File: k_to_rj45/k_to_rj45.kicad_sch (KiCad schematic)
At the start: 10 parts, among them J1 Conn_01x01_Female, J2 Conn_01x01_Female, J3 Conn_01x01_Female, J4 Conn_01x01_Female, J5 Conn_01x01_Female, J6 RJ45_Shielded, J7 Conn_01x01_Female, J8 Conn_01x01_Female

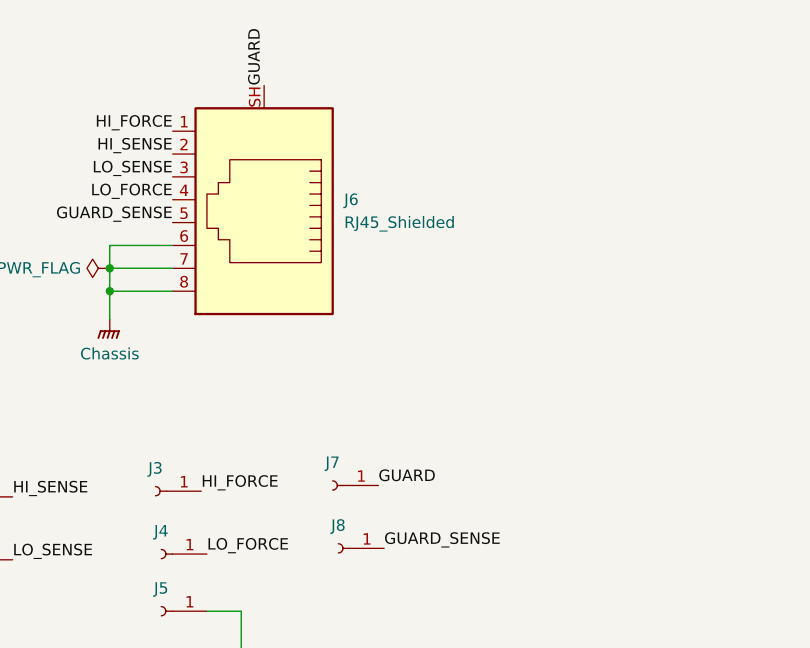
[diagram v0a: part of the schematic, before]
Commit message: update rj45 adapter and contact checker to v2
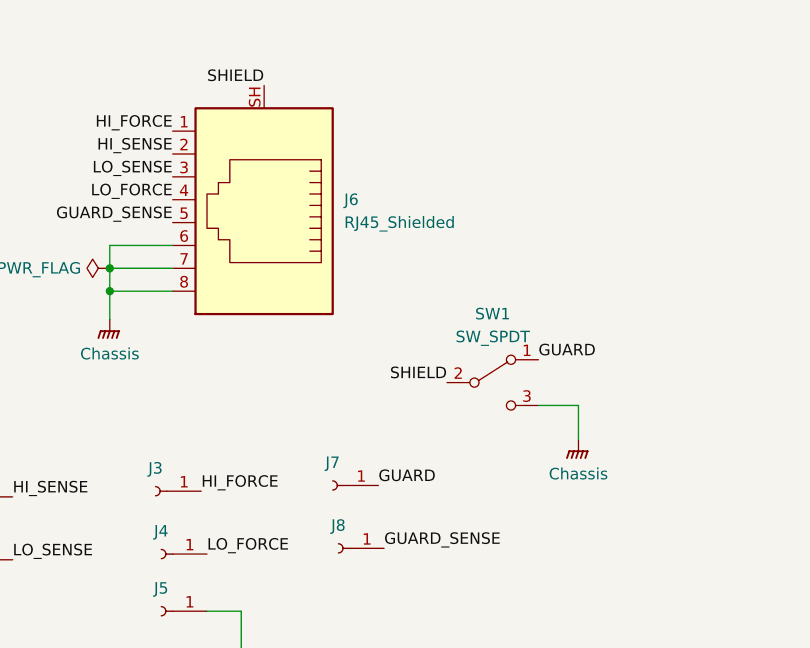
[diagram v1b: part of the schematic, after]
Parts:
- added SW1: SW_SPDT, custom_footprints:SPDT_slide_switch, symbol Switch:SW_SPDT
- J6: footprint Connector_RJ:RJ45_Wuerth_7499010001A_Horizontal -> custom_footprints:RJ45_TE_5557969-1_vertical_shield
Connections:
- net GNDPWR: now also SW1.3 (C)
- net GUARD: now also SW1.1 (A); no longer J6.SH
- new net SHIELD: J6.SH, SW1.2 (B)
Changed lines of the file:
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@@
+    (stroke (width 0) (type default) (color 0 0 0 0))
+  )
+  (wire (pts (xy 183.515 99.06) (xy 179.07 99.06))
+    (stroke (width 0) (type default) (color 0 0 0 0))
+  )
+  (wire (pts (xy 183.515 102.87) (xy 183.515 99.06))
     (stroke (width 0) (type default) (color 0 0 0 0))
   )
@@
     (effects (font (size 1.27 1.27)) (justify left bottom))
   )
+  (label "SHIELD" (at 148.59 63.5 180)
+    (effects (font (size 1.27 1.27)) (justify right bottom))
+  )
   (label "HI_FORCE" (at 141.605 108.585 0)
     (effects (font (size 1.27 1.27)) (justify left bottom))
@@
     (effects (font (size 1.27 1.27)) (justify left bottom))
   )
-  (label "GUARD" (at 148.59 63.5 90)
-    (effects (font (size 1.27 1.27)) (justify left bottom))
+  (label "SHIELD" (at 168.91 96.52 180)
+    (effects (font (size 1.27 1.27)) (justify right bottom))
+  )
+  (label "GUARD" (at 179.07 93.98 0)
+    (effects (font (size 1.27 1.27)) (justify left bottom))
+  )
+  (symbol (lib_id "power:GNDPWR") (at 183.515 102.87 0) (unit 1)
+    (in_bom yes) (on_board yes)
+    (property "Reference" "#PWR03" (id 0) (at 183.515 107.95 0)
+      (effects (font (size 1.27 1.27)) hide)
+    )
+    (property "Value" "GNDPWR" (id 1) (at 183.388 107.95 0)
+      (effects (font (size 1.27 1.27)) hide)
+    )
+    (property "Footprint" "" (id 2) (at 183.515 104.14 0)
+      (effects (font (size 1.27 1.27)) hide)
+    )
+    (property "Datasheet" "" (id 3) (at 183.515 104.14 0)
+      (effects (font (size 1.27 1.27)) hide)
+    )
+    (property "label" "Chassis" (id 4) (at 183.515 106.68 0))
+    (pin "1")
   )
   (symbol (lib_id "Connector:Conn_01x01_Female") (at 115.57 109.22 0) (mirror y) (unit 1)
@@
     (pin "1")
   )
+  (symbol (lib_id "Switch:SW_SPDT") (at 173.99 96.52 0) (unit 1)
+    (in_bom yes) (on_board yes) (fields_autoplaced)
+    (property "Reference" "SW1" (id 0) (at 173.99 88.9 0))
+    (property "Value" "SW_SPDT" (id 1) (at 173.99 91.44 0))
+    (property "Footprint" "custom_footprints:SPDT_slide_switch" (id 2) (at 173.99 96.52 0)
+      (effects (font (size 1.27 1.27)) hide)
+    )
+    (property "Datasheet" "~" (id 3) (at 173.99 96.52 0)
+      (effects (font (size 1.27 1.27)) hide)
+    )
+    (pin "1")
+    (pin "2")
+    (pin "3")
+  )
   (symbol (lib_id "Graphic:Logo_Open_Hardware_Small") (at 184.785 174.625 0) (unit 1)
     (in_bom yes) (on_board yes) (fields_autoplaced)
@@
   (symbol (lib_id "power:PWR_FLAG") (at 131.445 83.82 90) (unit 1)
     (in_bom yes) (on_board yes) (fields_autoplaced)
-    (property "Reference" "#FLG0101" (id 0) (at 129.54 83.82 0)
+    (property "Reference" "#FLG01" (id 0) (at 129.54 83.82 0)
       (effects (font (size 1.27 1.27)) hide)
     )
@@
       (effects (font (size 1.27 1.27)) (justify right))
     )
-    (property "Footprint" "Connector_RJ:RJ45_Wuerth_7499010001A_Horizontal" (id 2) (at 148.59 76.835 90)
+    (property "Footprint" "custom_footprints:RJ45_TE_5557969-1_vertical_shield" (id 2) (at 148.59 76.835 90)
       (effects (font (size 1.27 1.27)) hide)
     )
@@
   (symbol_instances
     (path "/791828a4-ec5a-4da3-b780-d1ef0a5a2f66"
-      (reference "#FLG0101") (unit 1) (value "PWR_FLAG") (footprint "")
+      (reference "#FLG01") (unit 1) (value "PWR_FLAG") (footprint "")
     )
     (path "/e7bd178b-6d10-4271-9032-e1c856b68c2c"
@@
       (reference "#PWR02") (unit 1) (value "GNDPWR") (footprint "")
     )
+    (path "/0caf96c1-61ed-415b-950b-ef8b402e7fa9"
+      (reference "#PWR03") (unit 1) (value "GNDPWR") (footprint "")
+    )
     (path "/340d8a86-2afc-4585-be63-6549052fe7df"
       (reference "J1") (unit 1) (value "Conn_01x01_Female") (footprint "custom_footprints:Mounting_Wuerth_WA-SMSI-4.5mm_H3mm_9774030482_pad_mod")
@@
     )
     (path "/7f4346e1-00d6-4bdf-95b7-67ca7d152f81"
-      (reference "J6") (unit 1) (value "RJ45_Shielded") (footprint "Connector_RJ:RJ45_Wuerth_7499010001A_Horizontal")
+      (reference "J6") (unit 1) (value "RJ45_Shielded") (footprint "custom_footprints:RJ45_TE_5557969-1_vertical_shield")
     )
     (path "/ffdef838-205b-464e-829a-c9b400e81c9d"
@@
       (reference "LOGO2") (unit 1) (value "Logo_Open_Hardware_Small") (footprint "custom_footprints:logo_small")
     )
-  )
+    (path "/5ce762db-cb92-4e90-ae28-7b5e827b4df0"
+      (reference "SW1") (unit 1) (value "SW_SPDT") (footprint "custom_footprints:SPDT_slide_switch")
+    )
+  )

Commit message: rev3 on contact checker boards
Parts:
- removed SW1: SW_SPDT, custom_footprints:SPDT_slide_switch, symbol Switch:SW_SPDT
- added SW1: SW_SPDT_MSM, custom_footprints:SPDT_slide_switch, symbol Switch:SW_SPDT_MSM
- J6: footprint custom_footprints:RJ45_TE_5557969-1_vertical_shield -> custom_footprints:RJ45_TE_100616-1_vertical_shield
- LOGO1, LOGO2: footprint custom_footprints:logo_small -> custom_footprints:logo
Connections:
- net GNDPWR: now also SW1.3; no longer J6.6
- net GUARD: now also J6.6, SW1.1
- net SHIELD: now also SW1.2
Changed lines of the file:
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@@
-    (stroke (width 0) (type default) (color 0 0 0 0))
-  )
-  (wire (pts (xy 138.43 81.28) (xy 131.445 81.28))
     (stroke (width 0) (type default) (color 0 0 0 0))
   )
@@
     (stroke (width 0) (type default) (color 0 0 0 0))
   )
-  (wire (pts (xy 131.445 81.28) (xy 131.445 83.82))
-    (stroke (width 0) (type default) (color 0 0 0 0))
-  )
   (wire (pts (xy 131.445 86.36) (xy 131.445 89.535))
     (stroke (width 0) (type default) (color 0 0 0 0))
   )
   (label "GUARD_SENSE" (at 138.43 78.74 180)
+    (effects (font (size 1.27 1.27)) (justify right bottom))
+  )
+  (label "GUARD" (at 138.43 81.28 180)
     (effects (font (size 1.27 1.27)) (justify right bottom))
   )
@@
     (pin "1")
   )
-  (symbol (lib_id "Switch:SW_SPDT") (at 173.99 96.52 0) (unit 1)
-    (in_bom yes) (on_board yes) (fields_autoplaced)
-    (property "Reference" "SW1" (id 0) (at 173.99 88.9 0))
-    (property "Value" "SW_SPDT" (id 1) (at 173.99 91.44 0))
+  (symbol (lib_id "Graphic:Logo_Open_Hardware_Small") (at 184.785 174.625 0) (unit 1)
+    (in_bom yes) (on_board yes) (fields_autoplaced)
+    (property "Reference" "LOGO1" (id 0) (at 184.785 167.64 0)
+      (effects (font (size 1.27 1.27)) hide)
+    )
+    (property "Value" "Logo_Open_Hardware_Small" (id 1) (at 184.785 180.34 0)
+      (effects (font (size 1.27 1.27)) hide)
+    )
+    (property "Footprint" "custom_footprints:logo" (id 2) (at 184.785 174.625 0)
+      (effects (font (size 1.27 1.27)) hide)
+    )
+    (property "Datasheet" "~" (id 3) (at 184.785 174.625 0)
+      (effects (font (size 1.27 1.27)) hide)
+    )
+  )
+  (symbol (lib_id "power:GNDPWR") (at 146.05 128.27 0) (unit 1)
+    (in_bom yes) (on_board yes)
+    (property "Reference" "#PWR02" (id 0) (at 146.05 133.35 0)
+      (effects (font (size 1.27 1.27)) hide)
+    )
+    (property "Value" "GNDPWR" (id 1) (at 145.923 133.35 0)
+      (effects (font (size 1.27 1.27)) hide)
+    )
+    (property "Footprint" "" (id 2) (at 146.05 129.54 0)
+      (effects (font (size 1.27 1.27)) hide)
+    )
+    (property "Datasheet" "" (id 3) (at 146.05 129.54 0)
+      (effects (font (size 1.27 1.27)) hide)
+    )
+    (property "label" "Chassis" (id 4) (at 146.05 132.08 0))
+    (pin "1")
+  )
+  (symbol (lib_id "Switch:SW_SPDT_MSM") (at 173.99 96.52 0) (unit 1)
+    (in_bom yes) (on_board yes) (fields_autoplaced)
+    (property "Reference" "SW1" (id 0) (at 174.117 88.265 0))
+    (property "Value" "SW_SPDT_MSM" (id 1) (at 174.117 90.805 0))
     (property "Footprint" "custom_footprints:SPDT_slide_switch" (id 2) (at 173.99 96.52 0)
       (effects (font (size 1.27 1.27)) hide)
     )
     (property "Datasheet" "~" (id 3) (at 173.99 96.52 0)
+      (effects (font (size 1.27 1.27)) hide)
+    )
+    (property "mfg part" "1103M2S3CQE2" (id 4) (at 173.99 96.52 0)
       (effects (font (size 1.27 1.27)) hide)
     )
@@
     (pin "3")
   )
-  (symbol (lib_id "Graphic:Logo_Open_Hardware_Small") (at 184.785 174.625 0) (unit 1)
-    (in_bom yes) (on_board yes) (fields_autoplaced)
-    (property "Reference" "LOGO1" (id 0) (at 184.785 167.64 0)
-      (effects (font (size 1.27 1.27)) hide)
-    )
-    (property "Value" "Logo_Open_Hardware_Small" (id 1) (at 184.785 180.34 0)
-      (effects (font (size 1.27 1.27)) hide)
-    )
-    (property "Footprint" "custom_footprints:logo_small" (id 2) (at 184.785 174.625 0)
-      (effects (font (size 1.27 1.27)) hide)
-    )
-    (property "Datasheet" "~" (id 3) (at 184.785 174.625 0)
-      (effects (font (size 1.27 1.27)) hide)
-    )
-  )
-  (symbol (lib_id "power:GNDPWR") (at 146.05 128.27 0) (unit 1)
-    (in_bom yes) (on_board yes)
-    (property "Reference" "#PWR02" (id 0) (at 146.05 133.35 0)
-      (effects (font (size 1.27 1.27)) hide)
-    )
-    (property "Value" "GNDPWR" (id 1) (at 145.923 133.35 0)
-      (effects (font (size 1.27 1.27)) hide)
-    )
-    (property "Footprint" "" (id 2) (at 146.05 129.54 0)
-      (effects (font (size 1.27 1.27)) hide)
-    )
-    (property "Datasheet" "" (id 3) (at 146.05 129.54 0)
-      (effects (font (size 1.27 1.27)) hide)
-    )
-    (property "label" "Chassis" (id 4) (at 146.05 132.08 0))
-    (pin "1")
-  )
   (symbol (lib_id "power:PWR_FLAG") (at 131.445 83.82 90) (unit 1)
     (in_bom yes) (on_board yes) (fields_autoplaced)
@@
       (effects (font (size 1.27 1.27)) (justify right))
     )
-    (property "Footprint" "custom_footprints:RJ45_TE_5557969-1_vertical_shield" (id 2) (at 148.59 76.835 90)
+    (property "Footprint" "custom_footprints:RJ45_TE_100616-1_vertical_shield" (id 2) (at 148.59 76.835 90)
       (effects (font (size 1.27 1.27)) hide)
     )
@@
       (effects (font (size 1.27 1.27)) hide)
     )
-    (property "Footprint" "custom_footprints:logo_small" (id 2) (at 276.86 174.625 0)
+    (property "Footprint" "custom_footprints:logo" (id 2) (at 276.86 174.625 0)
       (effects (font (size 1.27 1.27)) hide)
     )
@@
     )
     (path "/7f4346e1-00d6-4bdf-95b7-67ca7d152f81"
-      (reference "J6") (unit 1) (value "RJ45_Shielded") (footprint "custom_footprints:RJ45_TE_5557969-1_vertical_shield")
+      (reference "J6") (unit 1) (value "RJ45_Shielded") (footprint "custom_footprints:RJ45_TE_100616-1_vertical_shield")
     )
     (path "/ffdef838-205b-464e-829a-c9b400e81c9d"
@@
     )
     (path "/5e51672f-1c0c-4165-aae1-63bdb36319d8"
-      (reference "LOGO1") (unit 1) (value "Logo_Open_Hardware_Small") (footprint "custom_footprints:logo_small")
+      (reference "LOGO1") (unit 1) (value "Logo_Open_Hardware_Small") (footprint "custom_footprints:logo")
     )
     (path "/914145d2-f4f0-41b2-9d03-cea1c94d46e6"
-      (reference "LOGO2") (unit 1) (value "Logo_Open_Hardware_Small") (footprint "custom_footprints:logo_small")
-    )
-    (path "/5ce762db-cb92-4e90-ae28-7b5e827b4df0"
-      (reference "SW1") (unit 1) (value "SW_SPDT") (footprint "custom_footprints:SPDT_slide_switch")
-    )
-  )
+      (reference "LOGO2") (unit 1) (value "Logo_Open_Hardware_Small") (footprint "custom_footprints:logo")
+    )
+    (path "/6f601f1a-d32f-44dd-92ea-d916f14d237f"
+      (reference "SW1") (unit 1) (value "SW_SPDT_MSM") (footprint "custom_footprints:SPDT_slide_switch")
+    )
+  )

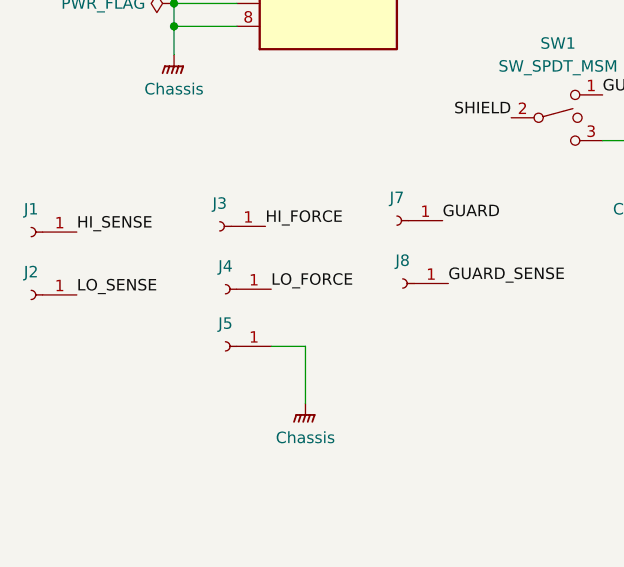
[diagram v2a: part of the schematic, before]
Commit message: new holder pcbs
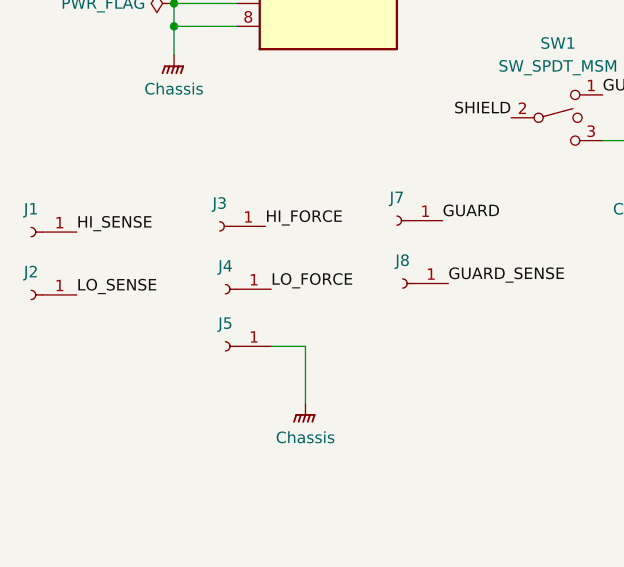
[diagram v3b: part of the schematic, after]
